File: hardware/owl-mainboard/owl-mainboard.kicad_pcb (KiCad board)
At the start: 4 copper layers, 61.8 x 79.8 mm, 106 parts, among them J101 Battery +, NTC, -, J201 USB-C, J202 EXP: GND, 3V3, A, B, J301 AMOLED FPC, J302 LRA, J303 DOCK: GND, VBUS, DET, GND, SW201 Ear left, SW202 Ear right, SW203 Beak, U101 BQ24073RGTR, U102 MAX17048G+T10, U103 TPS63802DLAR, U104 TPS22917DBVR, U201 ESP32-S3-WROOM-1-N16R8, U202 USBLC6-2SC6, U301 DRV2605LDGSR, U302 TMAG5273A2QDBVR, U303 LIS2DW12TR, U304 OPT3001DNPR, Y201 32.768kHz 12.5pF

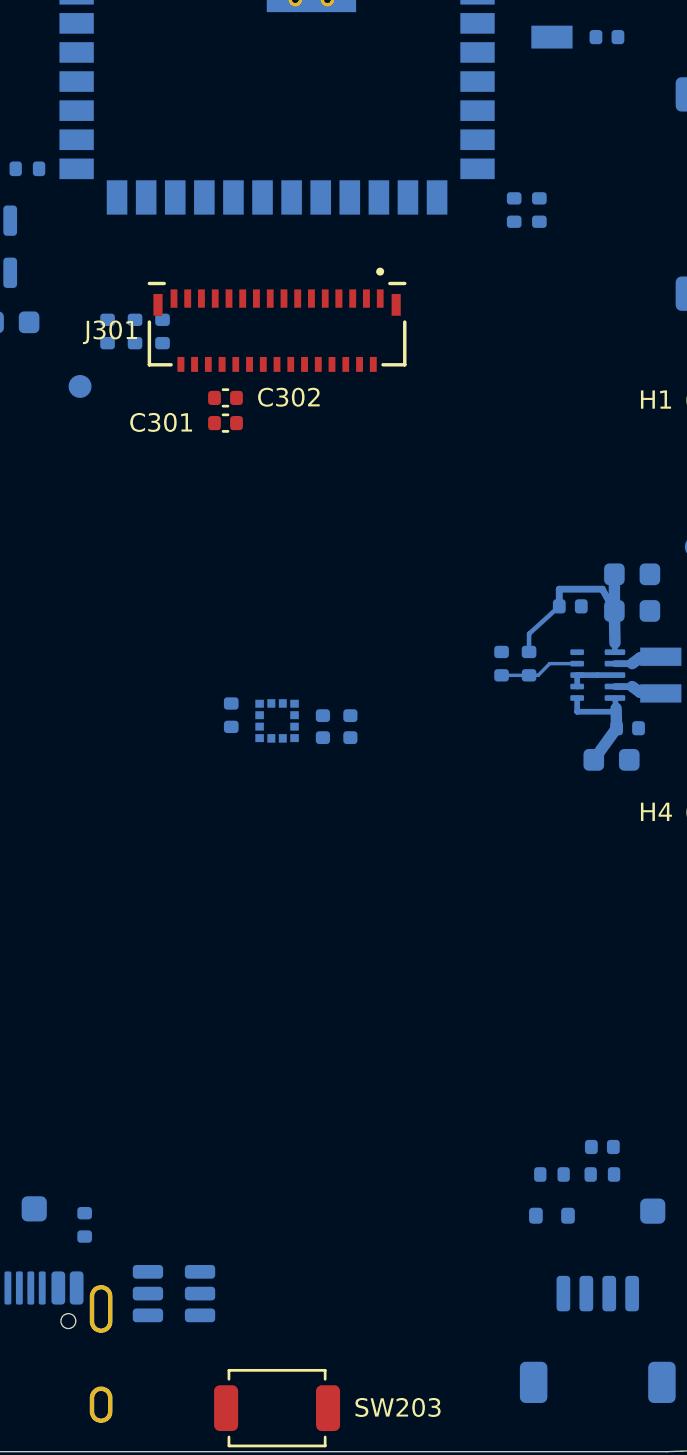
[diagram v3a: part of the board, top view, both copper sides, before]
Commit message: feat(hardware): route the USB pair from U202 to the ESP32-S3
USB_DP_CONN and USB_DM_CONN run through U202 under its body, then as a 0.2 mm pair with 0.15 mm
gap east, up a clear corridor at x 5.65/6.0 between the IMU and the TPS63802 divider, and into
R203/R204 from below, D+ on the left of travel at every turn so the lines never cross; USB_DP and
USB_DM are the short stubs to U201 pins 14 and 13. Lengths: D+ 62.6 + 2.5 mm, D- 64.2 + 4.9 mm
(full speed, no matching needed). The J201 fan-out to U202 is left for the next session. DRC: no
new violation type, 246 to 240 unconnected.
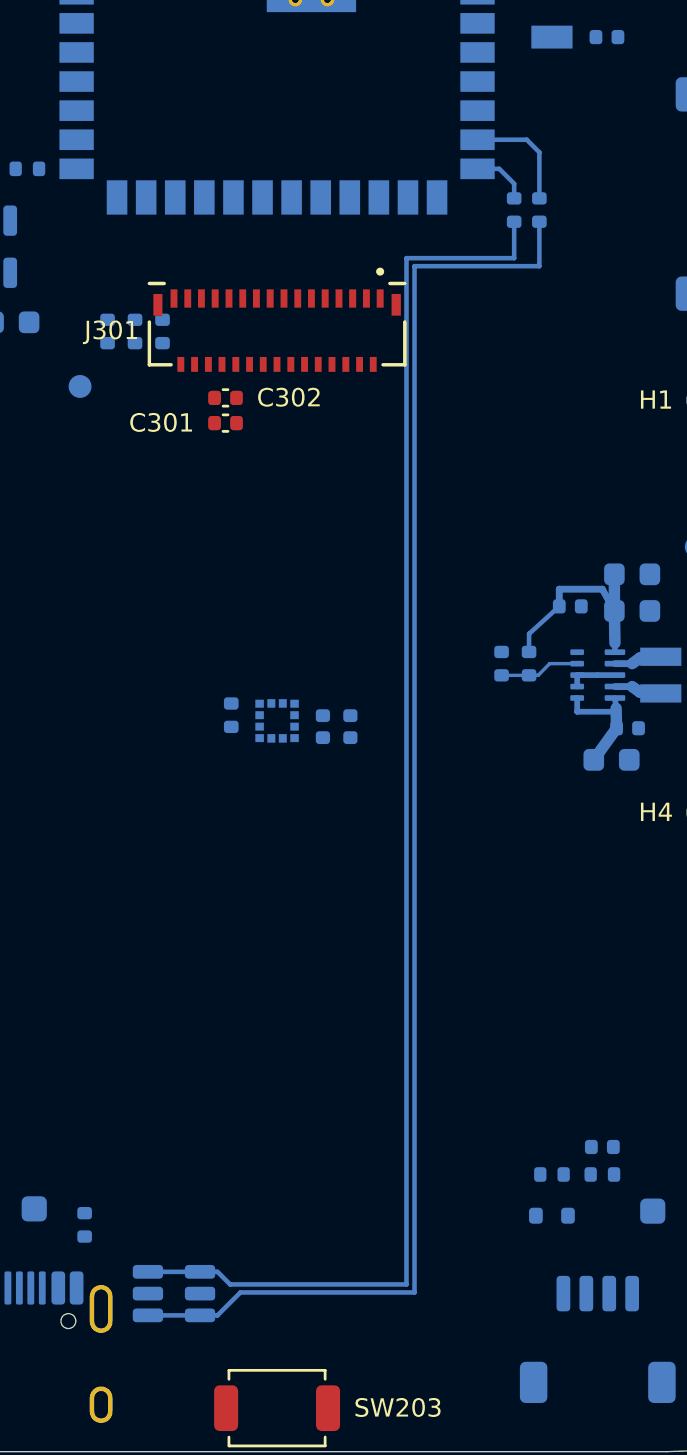
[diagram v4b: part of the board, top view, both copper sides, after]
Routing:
- net USB_DM_CONN: track 0.00 -> 64.2 mm
- net USB_DP_CONN: track 0.00 -> 62.6 mm
- net USB_DM: track 0.00 -> 4.94 mm
- net USB_DP: track 0.00 -> 2.51 mm
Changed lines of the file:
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@@
+	)
+	(segment
+		(start 96.64 129.05)
+		(end 97.4 129.05)
+		(width 0.2)
+		(locked yes)
+		(layer "B.Cu")
+		(net "USB_DP_CONN")
+	)
+	(segment
+		(start 94.36 129.05)
+		(end 96.64 129.05)
+		(width 0.2)
+		(locked yes)
+		(layer "B.Cu")
+		(net "USB_DP_CONN")
+	)
+	(segment
+		(start 110.35 84.8)
+		(end 110.35 83.21)
+		(width 0.2)
+		(locked yes)
+		(layer "B.Cu")
+		(net "USB_DP_CONN")
+	)
+	(segment
+		(start 105.65 129.6)
+		(end 105.65 84.8)
+		(width 0.2)
+		(locked yes)
+		(layer "B.Cu")
+		(net "USB_DP_CONN")
+	)
+	(segment
+		(start 97.4 129.05)
+		(end 97.95 129.6)
+		(width 0.2)
+		(locked yes)
+		(layer "B.Cu")
+		(net "USB_DP_CONN")
+	)
+	(segment
+		(start 105.65 84.8)
+		(end 110.35 84.8)
+		(width 0.2)
+		(locked yes)
+		(layer "B.Cu")
+		(net "USB_DP_CONN")
+	)
+	(segment
+		(start 97.95 129.6)
+		(end 105.65 129.6)
+		(width 0.2)
+		(locked yes)
+		(layer "B.Cu")
+		(net "USB_DP_CONN")
+	)
+	(segment
+		(start 98.4 129.949999)
+		(end 106 129.949999)
+		(width 0.2)
+		(locked yes)
+		(layer "B.Cu")
+		(net "USB_DM_CONN")
+	)
+	(segment
+		(start 97.4 130.949999)
+		(end 98.4 129.949999)
+		(width 0.2)
+		(locked yes)
+		(layer "B.Cu")
+		(net "USB_DM_CONN")
+	)
+	(segment
+		(start 106 129.949999)
+		(end 106 85.15)
+		(width 0.2)
+		(locked yes)
+		(layer "B.Cu")
+		(net "USB_DM_CONN")
+	)
+	(segment
+		(start 106 85.15)
+		(end 111.45 85.15)
+		(width 0.2)
+		(locked yes)
+		(layer "B.Cu")
+		(net "USB_DM_CONN")
+	)
+	(segment
+		(start 111.45 85.15)
+		(end 111.45 83.21)
+		(width 0.2)
+		(locked yes)
+		(layer "B.Cu")
+		(net "USB_DM_CONN")
+	)
+	(segment
+		(start 94.36 130.949999)
+		(end 96.64 130.949999)
+		(width 0.2)
+		(locked yes)
+		(layer "B.Cu")
+		(net "USB_DM_CONN")
+	)
+	(segment
+		(start 96.64 130.949999)
+		(end 97.4 130.949999)
+		(width 0.2)
+		(locked yes)
+		(layer "B.Cu")
+		(net "USB_DM_CONN")
 	)
 	(segment
@@
 		(net "TPS_L1")
 	)
+	(segment
+		(start 111.45 80.18)
+		(end 111.45 82.19)
+		(width 0.2)
+		(locked yes)
+		(layer "B.Cu")
+		(net "USB_DM")
+	)
+	(segment
+		(start 110.9 79.63)
+		(end 111.45 80.18)
+		(width 0.2)
+		(locked yes)
+		(layer "B.Cu")
+		(net "USB_DM")
+	)
+	(segment
+		(start 108.75 79.63)
+		(end 110.9 79.63)
+		(width 0.2)
+		(locked yes)
+		(layer "B.Cu")
+		(net "USB_DM")
+	)
+	(segment
+		(start 108.75 80.9)
+		(end 109.7 80.9)
+		(width 0.2)
+		(locked yes)
+		(layer "B.Cu")
+		(net "USB_DP")
+	)
+	(segment
+		(start 109.7 80.9)
+		(end 110.35 81.55)
+		(width 0.2)
+		(locked yes)
+		(layer "B.Cu")
+		(net "USB_DP")
+	)
+	(segment
+		(start 110.35 81.55)
+		(end 110.35 82.19)
+		(width 0.2)
+		(locked yes)
+		(layer "B.Cu")
+		(net "USB_DP")
+	)
 	(embedded_fonts no)

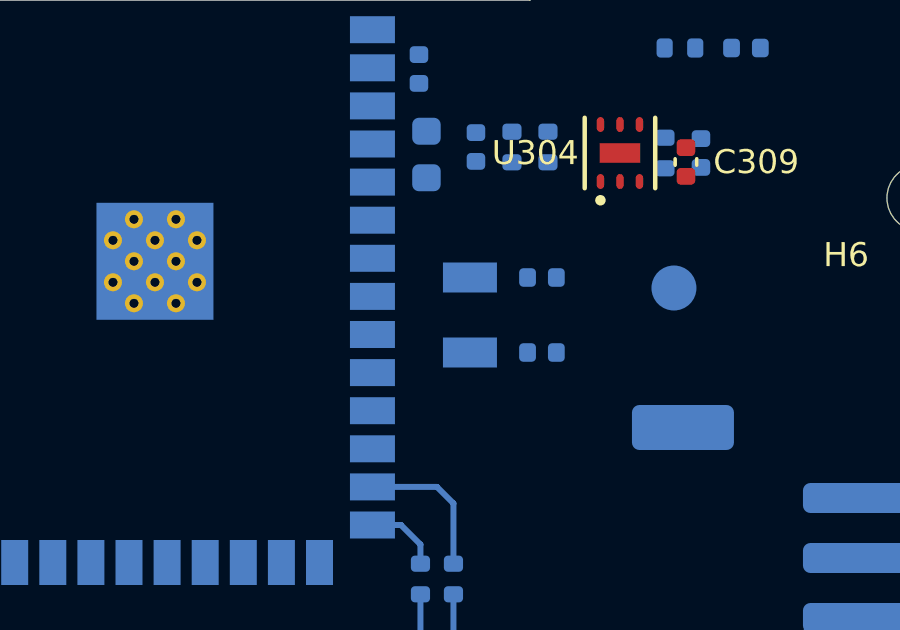
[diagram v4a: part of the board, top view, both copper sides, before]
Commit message: feat(hardware): route the 32.768 kHz crystal
U201 pins 8 and 9 run straight to Y201 (3.5 mm each, 0.15 mm), and on to the C204 and C205 load
caps on the crystal's far side (1.9 mm). Nothing else runs between the crystal and the module;
pins 7 and 10 have to escape another way when the rest is routed. hw_route.py also holds the
dock group, routed in the next commit. DRC: no new violation type, 240 to 236 unconnected.
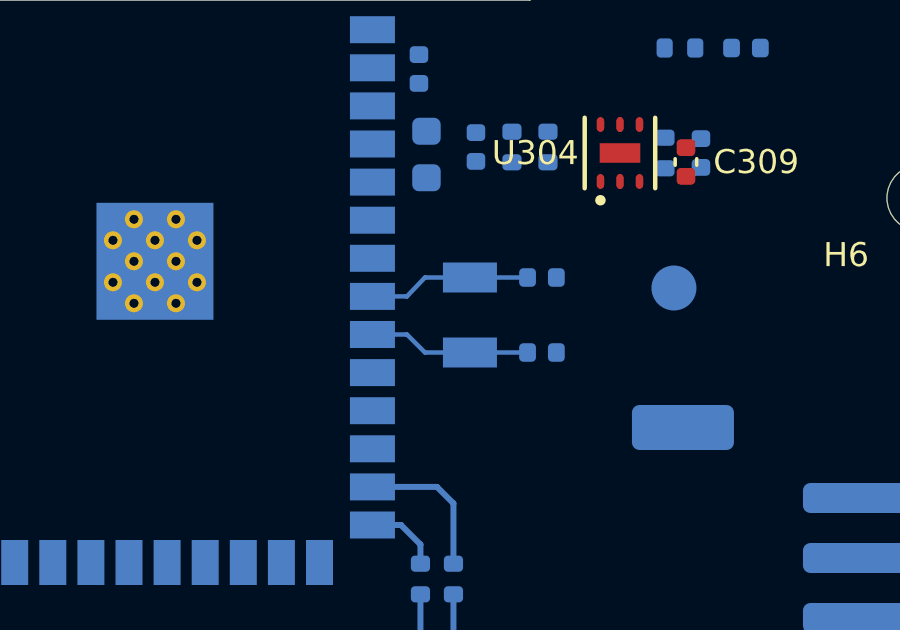
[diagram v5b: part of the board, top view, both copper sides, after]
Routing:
- net XTAL32_P: track 0.00 -> 5.44 mm
- net XTAL32_N: track 0.00 -> 5.42 mm
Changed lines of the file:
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@@
+	)
+	(segment
+		(start 109.9 73.28)
+		(end 110.5 72.65)
+		(width 0.15)
+		(locked yes)
+		(layer "B.Cu")
+		(net "XTAL32_P")
+	)
+	(segment
+		(start 108.75 73.28)
+		(end 109.9 73.28)
+		(width 0.15)
+		(locked yes)
+		(layer "B.Cu")
+		(net "XTAL32_P")
+	)
+	(segment
+		(start 112 72.65)
+		(end 113.92 72.65)
+		(width 0.15)
+		(locked yes)
+		(layer "B.Cu")
+		(net "XTAL32_P")
+	)
+	(segment
+		(start 110.5 72.65)
+		(end 112 72.65)
+		(width 0.15)
+		(locked yes)
+		(layer "B.Cu")
+		(net "XTAL32_P")
+	)
+	(segment
+		(start 109.9 74.55)
+		(end 110.5 75.15)
+		(width 0.15)
+		(locked yes)
+		(layer "B.Cu")
+		(net "XTAL32_N")
+	)
+	(segment
+		(start 108.75 74.55)
+		(end 109.9 74.55)
+		(width 0.15)
+		(locked yes)
+		(layer "B.Cu")
+		(net "XTAL32_N")
+	)
+	(segment
+		(start 112 75.15)
+		(end 113.92 75.15)
+		(width 0.15)
+		(locked yes)
+		(layer "B.Cu")
+		(net "XTAL32_N")
+	)
+	(segment
+		(start 110.5 75.15)
+		(end 112 75.15)
+		(width 0.15)
+		(locked yes)
+		(layer "B.Cu")
+		(net "XTAL32_N")
 	)
 	(segment

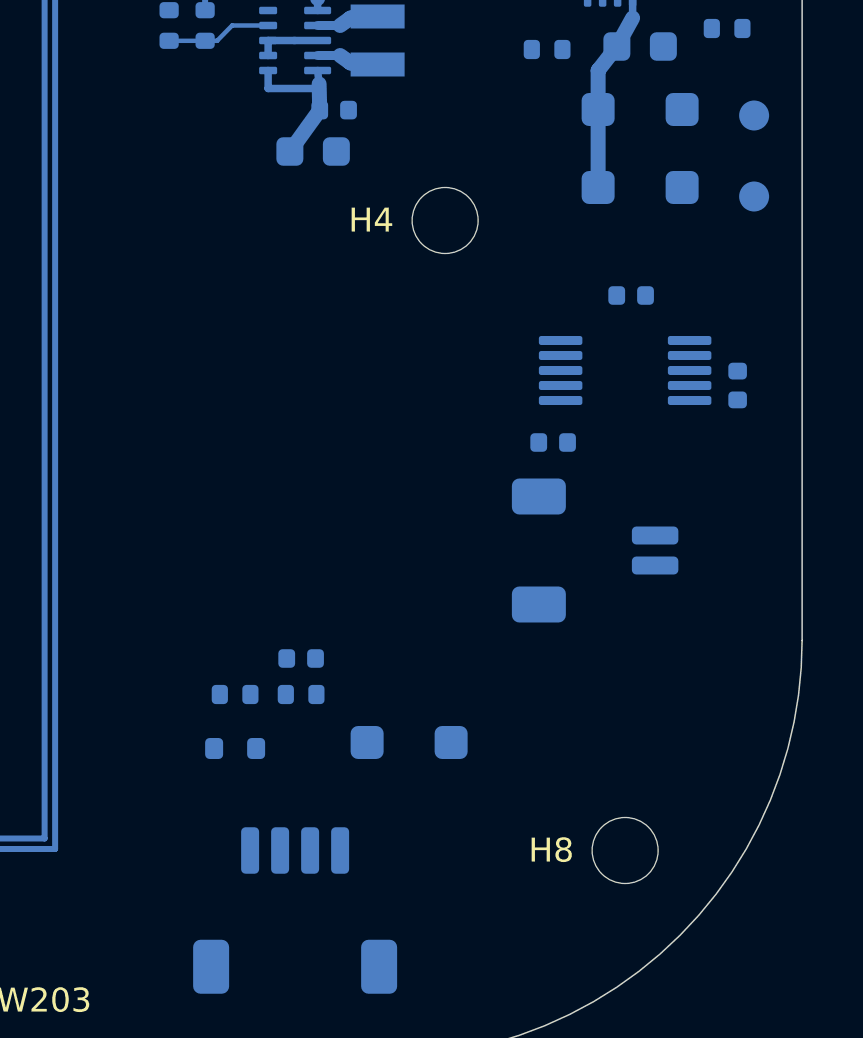
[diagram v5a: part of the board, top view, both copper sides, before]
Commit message: feat(hardware): route the dock power and pad lines
VBUS_DOCK runs from J303 pin 2 through the D301 TVS and up the right side, clear of the H4 boss
ring and U301, to the D102 anode at 0.5 mm (29.6 mm). DOCK_PAD runs from J303 pin 3 through the
D302 ESD diode to R307 (6.5 mm, 0.25 mm). DRC: no new violation type, 236 to 232 unconnected.
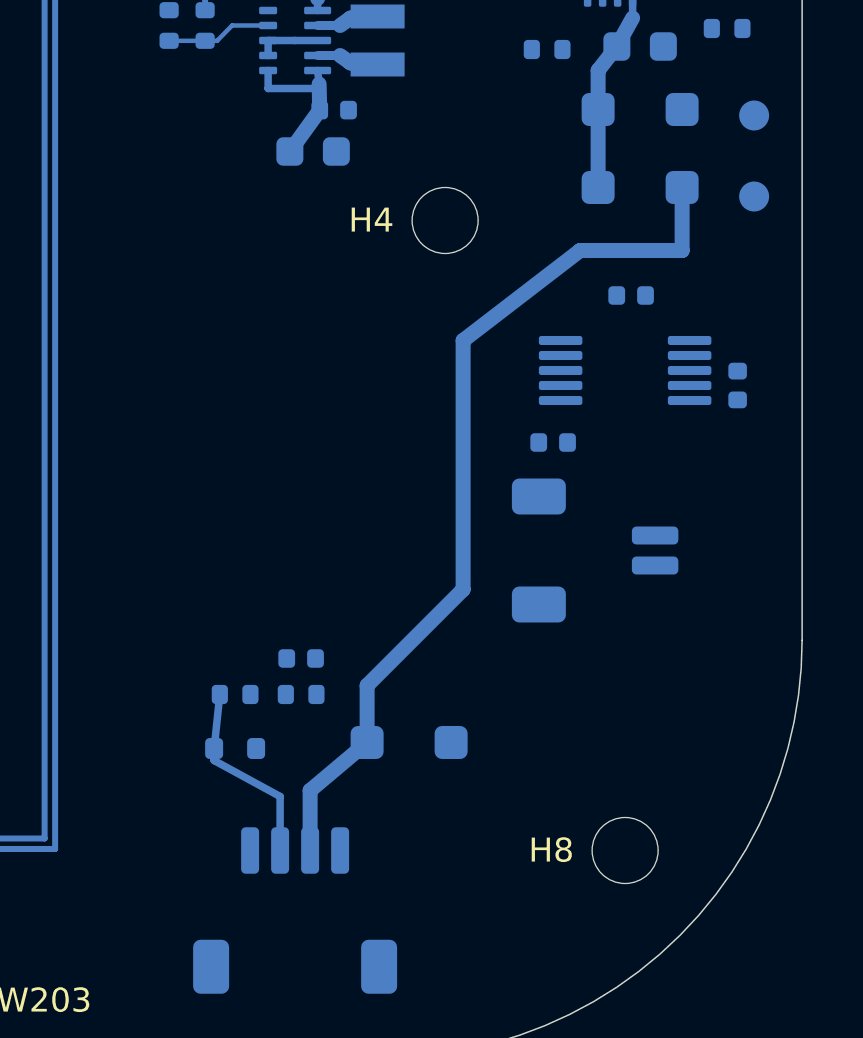
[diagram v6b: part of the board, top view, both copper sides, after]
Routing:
- net VBUS_DOCK: track 0.00 -> 29.6 mm
- net DOCK_PAD: track 0.00 -> 6.52 mm
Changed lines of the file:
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@@
+	)
+	(segment
+		(start 114.5 128)
+		(end 116.4 126.4)
+		(width 0.5)
+		(locked yes)
+		(layer "B.Cu")
+		(net "VBUS_DOCK")
+	)
+	(segment
+		(start 123.5 110)
+		(end 126.9 110)
+		(width 0.5)
+		(locked yes)
+		(layer "B.Cu")
+		(net "VBUS_DOCK")
+	)
+	(segment
+		(start 114.5 130)
+		(end 114.5 128)
+		(width 0.5)
+		(locked yes)
+		(layer "B.Cu")
+		(net "VBUS_DOCK")
+	)
+	(segment
+		(start 119.6 121.3)
+		(end 119.6 113)
+		(width 0.5)
+		(locked yes)
+		(layer "B.Cu")
+		(net "VBUS_DOCK")
+	)
+	(segment
+		(start 126.9 110)
+		(end 126.9 107.9)
+		(width 0.5)
+		(locked yes)
+		(layer "B.Cu")
+		(net "VBUS_DOCK")
+	)
+	(segment
+		(start 116.4 124.5)
+		(end 119.6 121.3)
+		(width 0.5)
+		(locked yes)
+		(layer "B.Cu")
+		(net "VBUS_DOCK")
+	)
+	(segment
+		(start 119.6 113)
+		(end 123.5 110)
+		(width 0.5)
+		(locked yes)
+		(layer "B.Cu")
+		(net "VBUS_DOCK")
+	)
+	(segment
+		(start 116.4 126.4)
+		(end 116.4 124.5)
+		(width 0.5)
+		(locked yes)
+		(layer "B.Cu")
+		(net "VBUS_DOCK")
+	)
+	(segment
+		(start 113.5 130)
+		(end 113.5 128.199999)
+		(width 0.25)
+		(locked yes)
+		(layer "B.Cu")
+		(net "DOCK_PAD")
+	)
+	(segment
+		(start 111.3 126.6)
+		(end 111.49 124.8)
+		(width 0.25)
+		(locked yes)
+		(layer "B.Cu")
+		(net "DOCK_PAD")
+	)
+	(segment
+		(start 113.5 128.199999)
+		(end 111.3 127)
+		(width 0.25)
+		(locked yes)
+		(layer "B.Cu")
+		(net "DOCK_PAD")
+	)
+	(segment
+		(start 111.3 127)
+		(end 111.3 126.6)
+		(width 0.25)
+		(locked yes)
+		(layer "B.Cu")
+		(net "DOCK_PAD")
 	)
 	(segment

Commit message: feat(hardware): route the USB-C fan-out to the ESD array
J201's D+ pads (A6, B6) drop to vias just above the pad row and its D- pads (A7, B7) to vias just
below it; each pair joins on F.Cu over the solid In1 GND and comes back up beside U202 pins 6 and
4 (0.2 mm, D+ 9.9 mm, D- 11.1 mm, three vias each). D- passes below the J201 peg hole and the
through-hole shell tab. B.Cu above the pads stays free for CC1, CC2 and VBUS. The USB nets are now
fully connected from J201 to U201. DRC: no new violation type, 232 to 228 unconnected.
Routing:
- net USB_DM_CONN: track 64.2 -> 75.4 mm, vias 0 -> 3
- net USB_DP_CONN: track 62.6 -> 72.5 mm, vias 0 -> 3
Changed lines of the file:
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@@
+	)
+	(segment
+		(start 88.25 128.4)
+		(end 93.3 128.75)
+		(width 0.2)
+		(locked yes)
+		(layer "F.Cu")
+		(net "USB_DP_CONN")
+	)
+	(segment
+		(start 87.25 128.4)
+		(end 88.25 128.4)
+		(width 0.2)
+		(locked yes)
+		(layer "F.Cu")
+		(net "USB_DP_CONN")
+	)
+	(via
+		(at 87.25 128.4)
+		(size 0.5)
+		(drill 0.3)
+		(layers "F.Cu" "B.Cu")
+		(locked yes)
+		(net "USB_DP_CONN")
+	)
+	(via
+		(at 88.25 128.4)
+		(size 0.5)
+		(drill 0.3)
+		(layers "F.Cu" "B.Cu")
+		(locked yes)
+		(net "USB_DP_CONN")
+	)
+	(via
+		(at 93.3 128.75)
+		(size 0.5)
+		(drill 0.3)
+		(layers "F.Cu" "B.Cu")
+		(locked yes)
+		(net "USB_DP_CONN")
 	)
 	(segment
@@
 	)
 	(segment
+		(start 87.25 129.755)
+		(end 87.25 128.4)
+		(width 0.2)
+		(locked yes)
+		(layer "B.Cu")
+		(net "USB_DP_CONN")
+	)
+	(segment
+		(start 88.25 129.755)
+		(end 88.25 128.4)
+		(width 0.2)
+		(locked yes)
+		(layer "B.Cu")
+		(net "USB_DP_CONN")
+	)
+	(segment
 		(start 105.65 129.6)
 		(end 105.65 84.8)
@@
 	)
 	(segment
+		(start 93.3 128.75)
+		(end 94.362 129.05)
+		(width 0.2)
+		(locked yes)
+		(layer "B.Cu")
+		(net "USB_DP_CONN")
+	)
+	(segment
+		(start 88.75 131.05)
+		(end 89.7 132.3)
+		(width 0.2)
+		(locked yes)
+		(layer "F.Cu")
+		(net "USB_DM_CONN")
+	)
+	(segment
+		(start 89.7 132.3)
+		(end 93.3 132.3)
+		(width 0.2)
+		(locked yes)
+		(layer "F.Cu")
+		(net "USB_DM_CONN")
+	)
+	(segment
+		(start 87.75 131.05)
+		(end 88.75 131.05)
+		(width 0.2)
+		(locked yes)
+		(layer "F.Cu")
+		(net "USB_DM_CONN")
+	)
+	(segment
+		(start 93.3 132.3)
+		(end 93.3 131)
+		(width 0.2)
+		(locked yes)
+		(layer "F.Cu")
+		(net "USB_DM_CONN")
+	)
+	(via
+		(at 88.75 131.05)
+		(size 0.5)
+		(drill 0.3)
+		(layers "F.Cu" "B.Cu")
+		(locked yes)
+		(net "USB_DM_CONN")
+	)
+	(via
+		(at 93.3 131)
+		(size 0.5)
+		(drill 0.3)
+		(layers "F.Cu" "B.Cu")
+		(locked yes)
+		(net "USB_DM_CONN")
+	)
+	(via
+		(at 87.75 131.05)
+		(size 0.5)
+		(drill 0.3)
+		(layers "F.Cu" "B.Cu")
+		(locked yes)
+		(net "USB_DM_CONN")
+	)
+	(segment
+		(start 87.75 129.755)
+		(end 87.75 131.05)
+		(width 0.2)
+		(locked yes)
+		(layer "B.Cu")
+		(net "USB_DM_CONN")
+	)
+	(segment
 		(start 98.4 129.949999)
 		(end 106 129.949999)
@@
 	)
 	(segment
+		(start 88.75 129.755)
+		(end 88.75 131.05)
+		(width 0.2)
+		(locked yes)
+		(layer "B.Cu")
+		(net "USB_DM_CONN")
+	)
+	(segment
 		(start 106 129.949999)
 		(end 106 85.15)
@@
 		(width 0.2)
 		(locked yes)
+		(layer "B.Cu")
+		(net "USB_DM_CONN")
+	)
+	(segment
+		(start 93.3 131)
+		(end 94.362 130.949999)
+		(width 0.2)
+		(locked yes)
